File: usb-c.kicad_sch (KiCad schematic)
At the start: 11 parts, among them IC1 TCPP01-M12, IC2 USBLC6-2SC6, IC3 632723100011, Q1 STL11N3LLH6

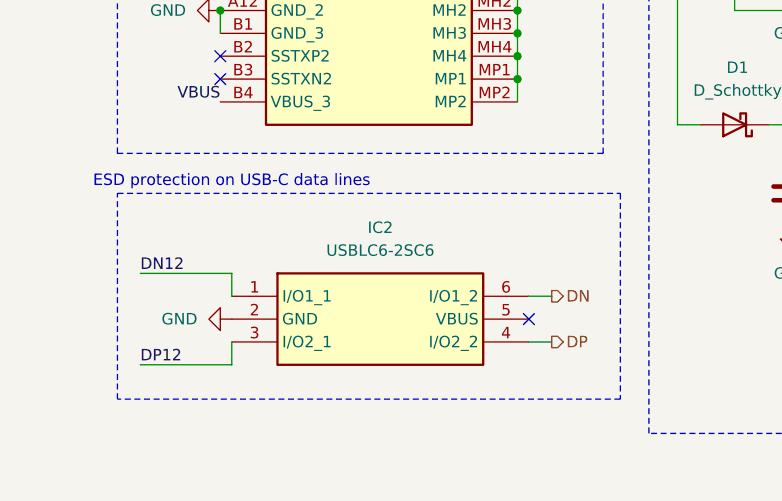
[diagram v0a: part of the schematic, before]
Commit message: Fix errors in synoptic and hierarchic pins
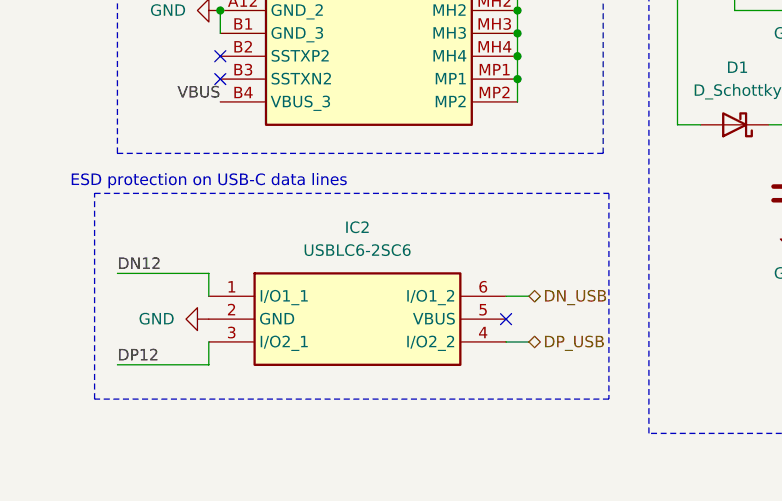
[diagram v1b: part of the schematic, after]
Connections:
- net DN renamed DN_USB
- net DP renamed DP_USB
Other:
- moved on the sheet: IC2
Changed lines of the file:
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@@
 	)
 	(rectangle
-		(start 82.55 114.3)
-		(end 138.43 137.16)
+		(start 80.01 114.3)
+		(end 137.16 137.16)
 		(stroke
 			(width 0)
@@
 	(text "ESD protection on USB-C data lines"
 		(exclude_from_sim no)
-		(at 95.25 113.03 0)
+		(at 92.71 113.03 0)
 		(effects
 			(font
@@
 	)
 	(no_connect
-		(at 128.27 128.27)
+		(at 125.73 128.27)
 	)
 	(wire
@@
 	(wire
 		(pts
-			(xy 95.25 133.35) (xy 95.25 130.81)
+			(xy 92.71 133.35) (xy 92.71 130.81)
 		)
 		(stroke
@@
 	(wire
 		(pts
-			(xy 95.25 123.19) (xy 95.25 125.73)
+			(xy 92.71 123.19) (xy 92.71 125.73)
 		)
 		(stroke
@@
 	(wire
 		(pts
-			(xy 130.81 125.73) (xy 128.27 125.73)
+			(xy 128.27 125.73) (xy 125.73 125.73)
 		)
 		(stroke
@@
 	(wire
 		(pts
-			(xy 130.81 130.81) (xy 128.27 130.81)
+			(xy 128.27 130.81) (xy 125.73 130.81)
 		)
 		(stroke
@@
 	(wire
 		(pts
-			(xy 85.09 133.35) (xy 95.25 133.35)
+			(xy 82.55 133.35) (xy 92.71 133.35)
 		)
 		(stroke
@@
 	(wire
 		(pts
-			(xy 85.09 123.19) (xy 95.25 123.19)
+			(xy 82.55 123.19) (xy 92.71 123.19)
 		)
 		(stroke
@@
 	)
 	(label "DN12"
-		(at 85.09 123.19 0)
+		(at 82.55 123.19 0)
 		(effects
 			(font
@@
 	)
 	(label "DP12"
-		(at 85.09 133.35 0)
+		(at 82.55 133.35 0)
 		(effects
 			(font
@@
 		)
 	)
-	(hierarchical_label "DP"
-		(shape output)
-		(at 130.81 130.81 0)
+	(hierarchical_label "DP_USB"
+		(shape bidirectional)
+		(at 128.27 130.81 0)
 		(effects
 			(font
@@
 		)
 	)
-	(hierarchical_label "DN"
-		(shape output)
-		(at 130.81 125.73 0)
+	(hierarchical_label "DN_USB"
+		(shape bidirectional)
+		(at 128.27 125.73 0)
 		(effects
 			(font
@@
 	(symbol
 		(lib_id "power:GND")
-		(at 95.25 128.27 270)
+		(at 92.71 128.27 270)
 		(unit 1)
 		(exclude_from_sim no)
@@
 		(fields_autoplaced yes)
 		(property "Reference" "#PWR01"
-			(at 88.9 128.27 0)
+			(at 86.36 128.27 0)
 			(effects
 				(font
@@
 		)
 		(property "Value" "GND"
-			(at 91.44 128.2699 90)
+			(at 88.9 128.2699 90)
 			(effects
 				(font
@@
 		)
 		(property "Footprint" ""
-			(at 95.25 128.27 0)
+			(at 92.71 128.27 0)
 			(effects
 				(font
@@
 		)
 		(property "Datasheet" ""
-			(at 95.25 128.27 0)
+			(at 92.71 128.27 0)
 			(effects
 				(font
@@
 		)
 		(property "Description" "Power symbol creates a global label with name \"GND\" , ground"
-			(at 95.25 128.27 0)
+			(at 92.71 128.27 0)
 			(effects
 				(font
@@
 	(symbol
 		(lib_id "weather-station-poc-sym:USBLC6-2SC6")
-		(at 95.25 125.73 0)
+		(at 92.71 125.73 0)
 		(unit 1)
 		(exclude_from_sim no)
@@
 		(fields_autoplaced yes)
 		(property "Reference" "IC2"
-			(at 111.76 118.11 0)
+			(at 109.22 118.11 0)
 			(effects
 				(font
@@
 		)
 		(property "Value" "USBLC6-2SC6"
-			(at 111.76 120.65 0)
+			(at 109.22 120.65 0)
 			(effects
 				(font
@@
 		)
 		(property "Footprint" "weather-station-poc-fp:SOT95P280X145-6N"
-			(at 124.46 220.65 0)
+			(at 121.92 220.65 0)
 			(effects
 				(font
@@
 		)
 		(property "Datasheet" "http://www.st.com/st-web-ui/static/active/en/resource/technical/document/datasheet/CD00050750.pdf"
-			(at 124.46 320.65 0)
+			(at 121.92 320.65 0)
 			(effects
 				(font
@@
 		)
 		(property "Description" "TVS Diode Array Uni-Directional USBLC6-2SC6 17V, SOT-23 6-Pin"
-			(at 95.25 125.73 0)
+			(at 92.71 125.73 0)
 			(effects
 				(font
@@
 		)
 		(property "Height" "1.45"
-			(at 124.46 520.65 0)
+			(at 121.92 520.65 0)
 			(effects
 				(font
@@
 		)
 		(property "Manufacturer_Name" "STMicroelectronics"
-			(at 124.46 620.65 0)
+			(at 121.92 620.65 0)
 			(effects
 				(font
@@
 		)
 		(property "Manufacturer_Part_Number" "USBLC6-2SC6"
-			(at 124.46 720.65 0)
+			(at 121.92 720.65 0)
 			(effects
 				(font
@@
 		)
 		(property "Mouser Part Number" "511-USBLC6-2SC6"
-			(at 124.46 820.65 0)
+			(at 121.92 820.65 0)
 			(effects
 				(font
@@
 		)
 		(property "Mouser Price/Stock" "https://www.mouser.co.uk/ProductDetail/STMicroelectronics/USBLC6-2SC6?qs=po45yt2pPpu%2FhNIlwQdTlg%3D%3D"
-			(at 124.46 920.65 0)
+			(at 121.92 920.65 0)
 			(effects
 				(font
@@
 		)
 		(property "Arrow Part Number" "USBLC6-2SC6"
-			(at 124.46 1020.65 0)
+			(at 121.92 1020.65 0)
 			(effects
 				(font
@@
 		)
 		(property "Arrow Price/Stock" "https://www.arrow.com/en/products/usblc6-2sc6/stmicroelectronics?utm_currency=USD&region=europe"
-			(at 124.46 1120.65 0)
-			(effects
-				(font
+			(at 121.92 1120.65 0)
+			(effects
+				(font

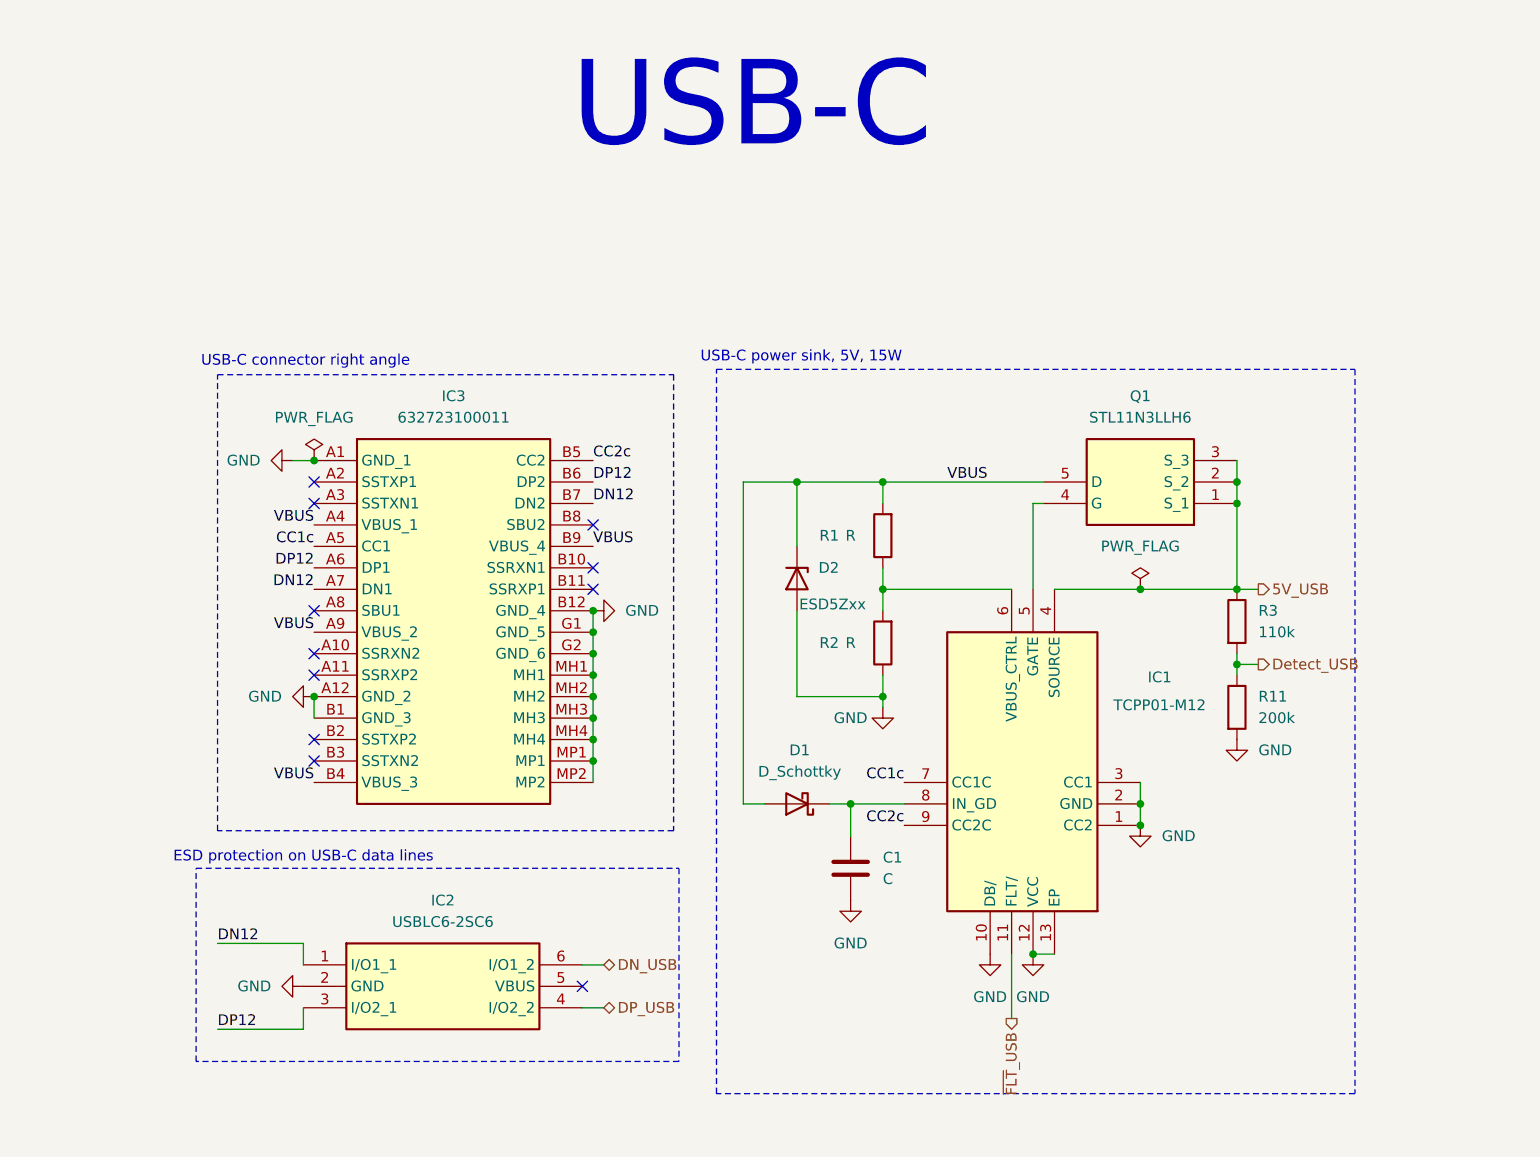
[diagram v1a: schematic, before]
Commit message: Add decoupling capacitors for USB C power sink
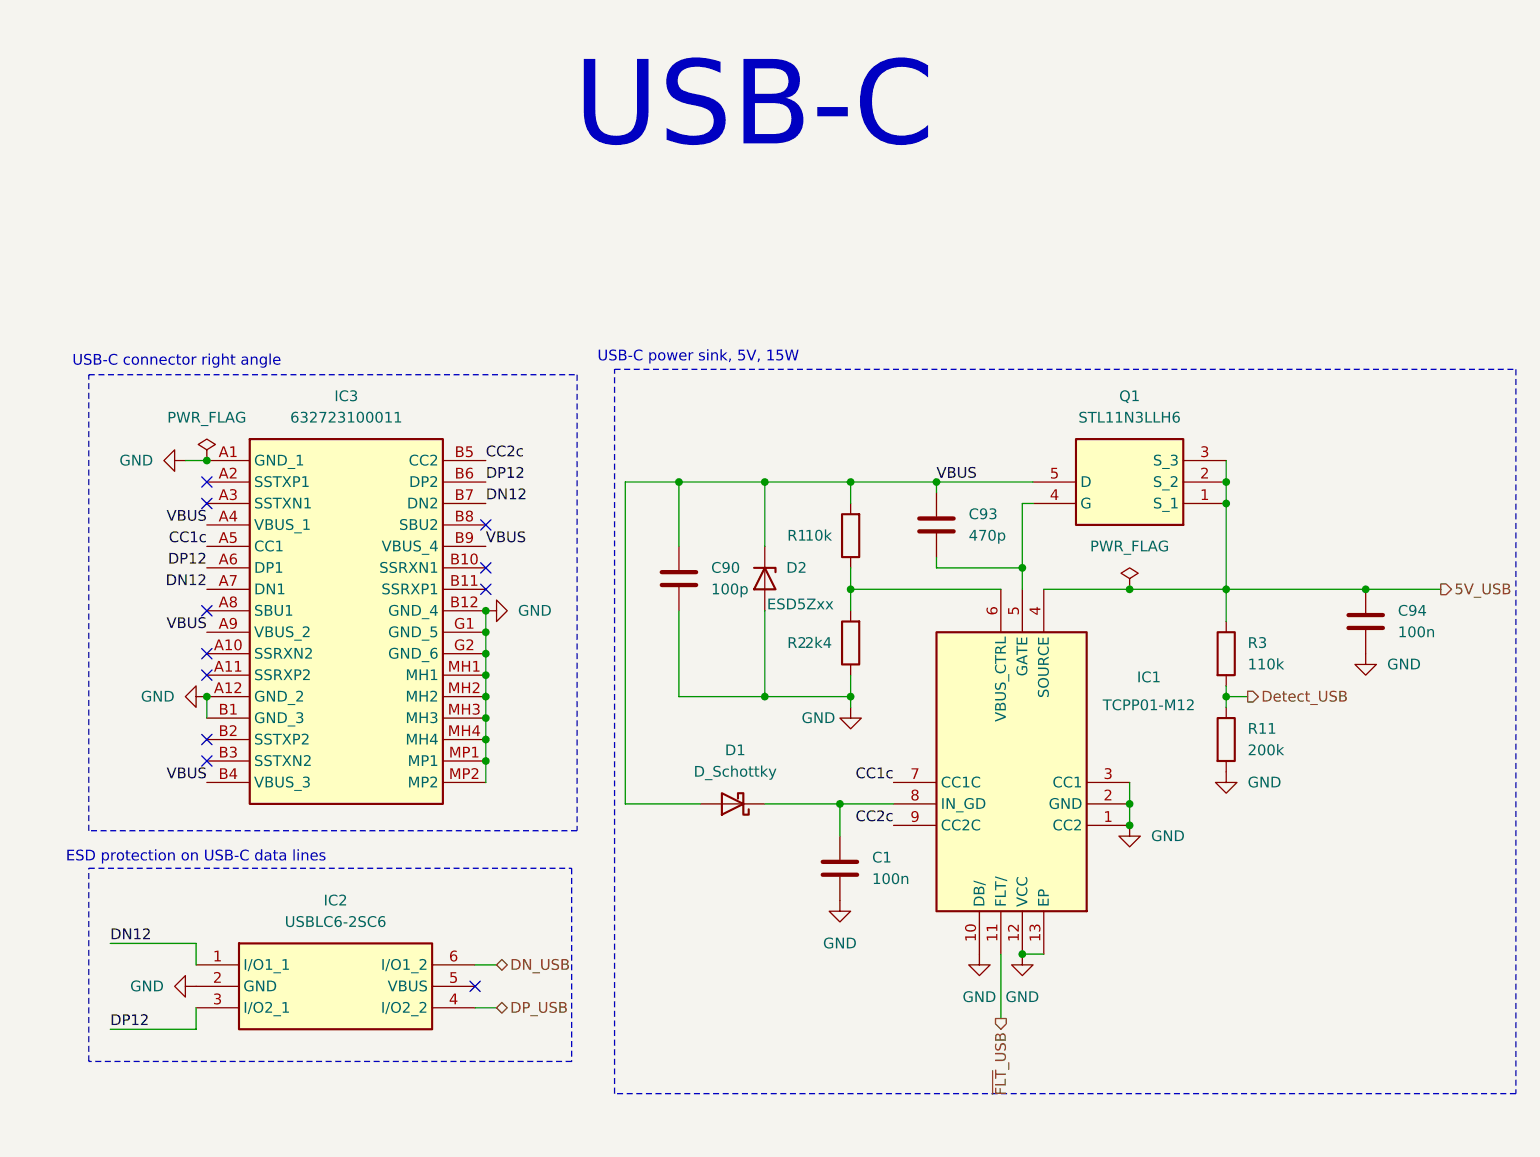
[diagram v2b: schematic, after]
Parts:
- added C90: 100p, Capacitor_SMD:C_0603_1608Metric_Pad1.08x0.95mm_HandSolder, symbol Device:C
- added C93: 470p, Capacitor_SMD:C_0603_1608Metric_Pad1.08x0.95mm_HandSolder, symbol Device:C
- added C94: 100n, Capacitor_SMD:C_0603_1608Metric_Pad1.08x0.95mm_HandSolder, symbol Device:C
- C1: value C -> 100n
- R1: value R -> 10k
- R2: value R -> 2k4
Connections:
- net 5V_USB: now also C94.1
- net GND: now also C90.2, C94.2
- net VBUS: now also C90.1, C93.1
- net at IC1.5 (GATE), Q1.4 (G): now also C93.2
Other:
- moved on the sheet: C1, D1, D2, IC1, IC2, IC3, Q1, R1, R11, R2, R3

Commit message: Fix some little warnings and refomat schematics files
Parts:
- renumbered C90 to C1, C1 to C2, C93 to C3, C94 to C4, IC2 to IC1, IC3 to IC2, IC1 to IC3, R11 to R4
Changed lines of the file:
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@@
 		(dnp no)
 		(fields_autoplaced yes)
-		(property "Reference" "#FLG02"
+		(property "Reference" "#FLG01"
 			(at 81.28 64.135 0)
 			(effects
@@
 			(project "weather-station-poc"
 				(path "/38eb53bb-294e-46e4-ad59-fd355ca373b9/336d3e95-9b5f-4d37-8b5a-efff814cf96e"
-					(reference "#FLG02")
+					(reference "#FLG01")
 					(unit 1)
 				)
@@
 		(dnp no)
 		(fields_autoplaced yes)
-		(property "Reference" "IC3"
+		(property "Reference" "IC2"
 			(at 97.79 58.42 0)
 			(effects
@@
 			(project "weather-station-poc"
 				(path "/38eb53bb-294e-46e4-ad59-fd355ca373b9/336d3e95-9b5f-4d37-8b5a-efff814cf96e"
-					(reference "IC3")
+					(reference "IC2")
 					(unit 1)
 				)
@@
 		(dnp no)
 		(fields_autoplaced yes)
-		(property "Reference" "R11"
+		(property "Reference" "R4"
 			(at 204.47 97.7899 0)
 			(effects
@@
 			(project "weather-station-poc"
 				(path "/38eb53bb-294e-46e4-ad59-fd355ca373b9/336d3e95-9b5f-4d37-8b5a-efff814cf96e"
-					(reference "R11")
+					(reference "R4")
 					(unit 1)
 				)
@@
 		(dnp no)
 		(fields_autoplaced yes)
-		(property "Reference" "C94"
+		(property "Reference" "C4"
 			(at 222.25 83.8199 0)
 			(effects
@@
 			(project "weather-station-poc"
 				(path "/38eb53bb-294e-46e4-ad59-fd355ca373b9/336d3e95-9b5f-4d37-8b5a-efff814cf96e"
-					(reference "C94")
+					(reference "C4")
 					(unit 1)
 				)
@@
 		(dnp no)
 		(fields_autoplaced yes)
-		(property "Reference" "#PWR01"
+		(property "Reference" "#PWR014"
 			(at 73.66 128.27 0)
 			(effects
@@
 			(project "weather-station-poc"
 				(path "/38eb53bb-294e-46e4-ad59-fd355ca373b9/336d3e95-9b5f-4d37-8b5a-efff814cf96e"
-					(reference "#PWR01")
+					(reference "#PWR014")
 					(unit 1)
 				)
@@
 		(dnp no)
 		(fields_autoplaced yes)
-		(property "Reference" "C93"
+		(property "Reference" "C3"
 			(at 171.45 72.3899 0)
 			(effects
@@
 			(project "weather-station-poc"
 				(path "/38eb53bb-294e-46e4-ad59-fd355ca373b9/336d3e95-9b5f-4d37-8b5a-efff814cf96e"
-					(reference "C93")
+					(reference "C3")
 					(unit 1)
 				)
@@
 		(dnp no)
 		(fields_autoplaced yes)
-		(property "Reference" "#PWR09"
+		(property "Reference" "#PWR013"
 			(at 72.39 66.04 0)
 			(effects
@@
 			(project "weather-station-poc"
 				(path "/38eb53bb-294e-46e4-ad59-fd355ca373b9/336d3e95-9b5f-4d37-8b5a-efff814cf96e"
-					(reference "#PWR09")
+					(reference "#PWR013")
 					(unit 1)
 				)
@@
 		(dnp no)
 		(fields_autoplaced yes)
-		(property "Reference" "#PWR04"
+		(property "Reference" "#PWR022"
 			(at 201.93 109.22 0)
 			(effects
@@
 			(project "weather-station-poc"
 				(path "/38eb53bb-294e-46e4-ad59-fd355ca373b9/336d3e95-9b5f-4d37-8b5a-efff814cf96e"
-					(reference "#PWR04")
+					(reference "#PWR022")
 					(unit 1)
 				)
@@
 		(dnp no)
 		(fields_autoplaced yes)
-		(property "Reference" "#PWR0153"
+		(property "Reference" "#PWR023"
 			(at 218.44 95.25 0)
 			(effects
@@
 			(project "weather-station-poc"
 				(path "/38eb53bb-294e-46e4-ad59-fd355ca373b9/336d3e95-9b5f-4d37-8b5a-efff814cf96e"
-					(reference "#PWR0153")
+					(reference "#PWR023")
 					(unit 1)
 				)
@@
 		(dnp no)
 		(fields_autoplaced yes)
-		(property "Reference" "C1"
+		(property "Reference" "C2"
 			(at 160.02 113.0299 0)
 			(effects
@@
 			(project "weather-station-poc"
 				(path "/38eb53bb-294e-46e4-ad59-fd355ca373b9/336d3e95-9b5f-4d37-8b5a-efff814cf96e"
-					(reference "C1")
+					(reference "C2")
 					(unit 1)
 				)
@@
 		(on_board yes)
 		(dnp no)
-		(property "Reference" "IC1"
+		(property "Reference" "IC3"
 			(at 192.786 91.694 0)
 			(effects
@@
 			(project "weather-station-poc"
 				(path "/38eb53bb-294e-46e4-ad59-fd355ca373b9/336d3e95-9b5f-4d37-8b5a-efff814cf96e"
-					(reference "IC1")
+					(reference "IC3")
 					(unit 1)
 				)
@@
 		(dnp no)
 		(fields_autoplaced yes)
-		(property "Reference" "#PWR06"
+		(property "Reference" "#PWR016"
 			(at 120.65 83.82 0)
 			(effects
@@
 			(project "weather-station-poc"
 				(path "/38eb53bb-294e-46e4-ad59-fd355ca373b9/336d3e95-9b5f-4d37-8b5a-efff814cf96e"
-					(reference "#PWR06")
+					(reference "#PWR016")
 					(unit 1)
 				)
@@
 		(dnp no)
 		(fields_autoplaced yes)
-		(property "Reference" "#PWR05"
+		(property "Reference" "#PWR017"
 			(at 156.21 124.46 0)
 			(effects
@@
 			(project "weather-station-poc"
 				(path "/38eb53bb-294e-46e4-ad59-fd355ca373b9/336d3e95-9b5f-4d37-8b5a-efff814cf96e"
-					(reference "#PWR05")
+					(reference "#PWR017")
 					(unit 1)
 				)
@@
 		(on_board yes)
 		(dnp no)
-		(property "Reference" "#PWR03"
+		(property "Reference" "#PWR018"
 			(at 157.48 101.6 0)
 			(effects
@@
 			(project "weather-station-poc"
 				(path "/38eb53bb-294e-46e4-ad59-fd355ca373b9/336d3e95-9b5f-4d37-8b5a-efff814cf96e"
-					(reference "#PWR03")
+					(reference "#PWR018")
 					(unit 1)
 				)
@@
 		(dnp no)
 		(fields_autoplaced yes)
-		(property "Reference" "#PWR049"
+		(property "Reference" "#PWR020"
 			(at 177.8 130.81 0)
 			(effects
@@
 			(project "weather-station-poc"
 				(path "/38eb53bb-294e-46e4-ad59-fd355ca373b9/336d3e95-9b5f-4d37-8b5a-efff814cf96e"
-					(reference "#PWR049")
+					(reference "#PWR020")
 					(unit 1)
 				)
@@
 		(dnp no)
 		(fields_autoplaced yes)
-		(property "Reference" "C90"
+		(property "Reference" "C1"
 			(at 140.97 78.7399 0)
 			(effects
@@
 			(project "weather-station-poc"
 				(path "/38eb53bb-294e-46e4-ad59-fd355ca373b9/336d3e95-9b5f-4d37-8b5a-efff814cf96e"
-					(reference "C90")
+					(reference "C1")
 					(unit 1)
 				)
@@
 		(dnp no)
 		(fields_autoplaced yes)
-		(property "Reference" "#PWR010"
+		(property "Reference" "#PWR015"
 			(at 74.93 93.98 0)
 			(effects
@@
 			(project "weather-station-poc"
 				(path "/38eb53bb-294e-46e4-ad59-fd355ca373b9/336d3e95-9b5f-4d37-8b5a-efff814cf96e"
-					(reference "#PWR010")
+					(reference "#PWR015")
 					(unit 1)
 				)
@@
 		(dnp no)
 		(fields_autoplaced yes)
-		(property "Reference" "#FLG01"
+		(property "Reference" "#FLG02"
 			(at 190.5 79.375 0)
 			(effects
@@
 			(project "weather-station-poc"
 				(path "/38eb53bb-294e-46e4-ad59-fd355ca373b9/336d3e95-9b5f-4d37-8b5a-efff814cf96e"
-					(reference "#FLG01")
+					(reference "#FLG02")
 					(unit 1)
 				)
@@
 		(dnp no)
 		(fields_autoplaced yes)
-		(property "Reference" "#PWR02"
+		(property "Reference" "#PWR021"
 			(at 190.5 115.57 0)
 			(effects
@@
 			(project "weather-station-poc"
 				(path "/38eb53bb-294e-46e4-ad59-fd355ca373b9/336d3e95-9b5f-4d37-8b5a-efff814cf96e"
-					(reference "#PWR02")
+					(reference "#PWR021")
 					(unit 1)
 				)
@@
 		(dnp no)
 		(fields_autoplaced yes)
-		(property "Reference" "IC2"
+		(property "Reference" "IC1"
 			(at 96.52 118.11 0)
 			(effects
@@
 			(project "weather-station-poc"
 				(path "/38eb53bb-294e-46e4-ad59-fd355ca373b9/336d3e95-9b5f-4d37-8b5a-efff814cf96e"
-					(reference "IC2")
+					(reference "IC1")
 					(unit 1)
 				)
@@
 		(dnp no)
 		(fields_autoplaced yes)
-		(property "Reference" "#PWR050"
+		(property "Reference" "#PWR019"
 			(at 172.72 130.81 0)
 			(effects
@@
 			(project "weather-station-poc"
 				(path "/38eb53bb-294e-46e4-ad59-fd355ca373b9/336d3e95-9b5f-4d37-8b5a-efff814cf96e"
-					(reference "#PWR050")
-					(unit 1)
-				)
+					(reference "#PWR019")
+					(unit 1)
+				)

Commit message: Assign 0603 footprints to all resistors
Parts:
- R3, R4: footprint (none) -> Resistor_SMD:R_0603_1608Metric_Pad0.98x0.95mm_HandSolder
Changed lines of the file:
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@@
 			)
 		)
-		(property "Footprint" ""
+		(property "Footprint" "Resistor_SMD:R_0603_1608Metric_Pad0.98x0.95mm_HandSolder"
 			(at 200.152 99.06 90)
 			(effects
@@
 			)
 		)
-		(property "Footprint" ""
+		(property "Footprint" "Resistor_SMD:R_0603_1608Metric_Pad0.98x0.95mm_HandSolder"
 			(at 200.152 88.9 90)
 			(effects

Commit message: Use preconised diodes for USB-C by ST
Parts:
- removed D1: D_Schottky, Diode_SMD:D_SOD-123F, symbol Device:D_Schottky
- removed D2: ESD5Zxx, Diode_SMD:D_SOD-523, symbol Diode:ESD5Zxx
- added D1: ESDA25P35-1U1M, weather-station-poc-fp:ESDA25P351U1M, symbol weather-station-poc-sym:ESDA25P35-1U1M
- added D2: BAT54KFILM, weather-station-poc-fp:SODFL1608X70N, symbol weather-station-poc-sym:BAT54KFILM
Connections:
- net GND: now also D1.2 (A)
- net VBUS: now also D1.1 (K), D2.2 (A)
- net at C2.1, IC3.8 (IN_GD): now also D2.1 (K)
